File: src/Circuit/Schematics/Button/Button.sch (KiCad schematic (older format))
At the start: 5 parts

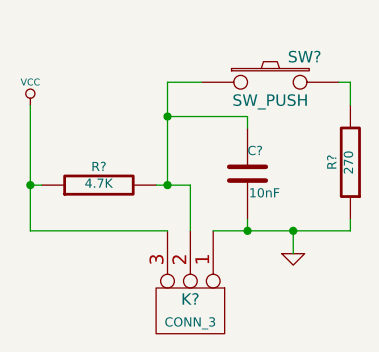
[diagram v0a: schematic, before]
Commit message: Created button circuit
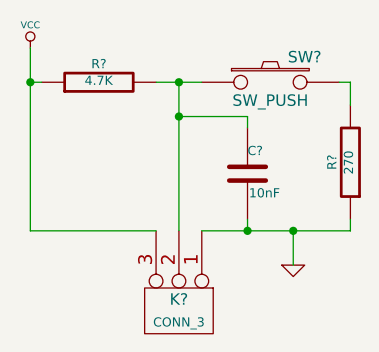
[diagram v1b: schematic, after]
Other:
- moved on the sheet: K?, R?
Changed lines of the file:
@@
 L GND #PWR?
 U 1 1 54819BC6
-P 5900 4900
-F 0 "#PWR?" H 5900 4900 30  0001 C CNN
-F 1 "GND" H 5900 4830 30  0001 C CNN
-F 2 "~" H 5900 4900 60  0000 C CNN
-F 3 "~" H 5900 4900 60  0000 C CNN
-	1    5900 4900
+P 5900 4950
+F 0 "#PWR?" H 5900 4950 30  0001 C CNN
+F 1 "GND" H 5900 4880 30  0001 C CNN
+F 2 "~" H 5900 4950 60  0000 C CNN
+F 3 "~" H 5900 4950 60  0000 C CNN
+	1    5900 4950
 	1    0    0    -1
 $EndComp
@@
 L CONN_3 K?
 U 1 1 54819CEA
-P 5450 5150
-F 0 "K?" V 5400 5150 50  0000 C CNN
-F 1 "CONN_3" V 5500 5150 40  0000 C CNN
-F 2 "~" H 5450 5150 60  0000 C CNN
-F 3 "~" H 5450 5150 60  0000 C CNN
-	1    5450 5150
+P 5400 5150
+F 0 "K?" V 5350 5150 50  0000 C CNN
+F 1 "CONN_3" V 5450 5150 40  0000 C CNN
+F 2 "~" H 5400 5150 60  0000 C CNN
+F 3 "~" H 5400 5150 60  0000 C CNN
+	1    5400 5150
 	0    1    1    0
 $EndComp
@@
 L R R?
 U 1 1 54819D40
-P 5050 4600
-F 0 "R?" V 5130 4600 40  0000 C CNN
-F 1 "4.7K" V 5057 4601 40  0000 C CNN
-F 2 "~" V 4980 4600 30  0000 C CNN
-F 3 "~" H 5050 4600 30  0000 C CNN
-	1    5050 4600
+P 5050 4150
+F 0 "R?" V 5130 4150 40  0000 C CNN
+F 1 "4.7K" V 5057 4151 40  0000 C CNN
+F 2 "~" V 4980 4150 30  0000 C CNN
+F 3 "~" H 5050 4150 30  0000 C CNN
+	1    5050 4150
 	0    -1   -1   0
 $EndComp
@@
 L VCC #PWR?
 U 1 1 5481A581
-P 4750 4250
-F 0 "#PWR?" H 4750 4350 30  0001 C CNN
-F 1 "VCC" H 4750 4350 30  0000 C CNN
-F 2 "~" H 4750 4250 60  0000 C CNN
-F 3 "~" H 4750 4250 60  0000 C CNN
-	1    4750 4250
+P 4750 4000
+F 0 "#PWR?" H 4750 4100 30  0001 C CNN
+F 1 "VCC" H 4750 4100 30  0000 C CNN
+F 2 "~" H 4750 4000 60  0000 C CNN
+F 3 "~" H 4750 4000 60  0000 C CNN
+	1    4750 4000
 	1    0    0    -1
 $EndComp
@@
 	6150 4800 6150 4750
 Wire Wire Line
-	5550 4800 6150 4800
+	5500 4800 6150 4800
 Wire Wire Line
-	4750 4800 5350 4800
+	4750 4000 4750 4800
 Wire Wire Line
-	4750 4250 4750 4800
-Wire Wire Line
-	5900 4800 5900 4900
+	5900 4800 5900 4950
 Connection ~ 5900 4800
 Wire Wire Line
-	4800 4600 4750 4600
-Connection ~ 4750 4600
-Wire Wire Line
-	5450 4800 5450 4600
-Wire Wire Line
-	5450 4600 5300 4600
-Wire Wire Line
-	5350 4600 5350 4150
-Wire Wire Line
-	5350 4150 5500 4150
-Connection ~ 5350 4600
-Wire Wire Line
-	5350 4300 5700 4300
+	5300 4150 5500 4150
 Wire Wire Line
 	5700 4300 5700 4350
-Connection ~ 5350 4300
 Wire Wire Line
 	5700 4750 5700 4800
@@
 Wire Wire Line
 	6100 4150 6150 4150
+Wire Wire Line
+	4800 4150 4750 4150
+Connection ~ 4750 4150
+Wire Wire Line
+	5400 4800 5400 4150
+Connection ~ 5400 4150
+Wire Wire Line
+	4750 4800 5300 4800
+Wire Wire Line
+	5700 4300 5400 4300
+Connection ~ 5400 4300
 $EndSCHEMATC
